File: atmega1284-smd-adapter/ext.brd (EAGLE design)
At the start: 37.6 x 55.9 mm, 5 parts

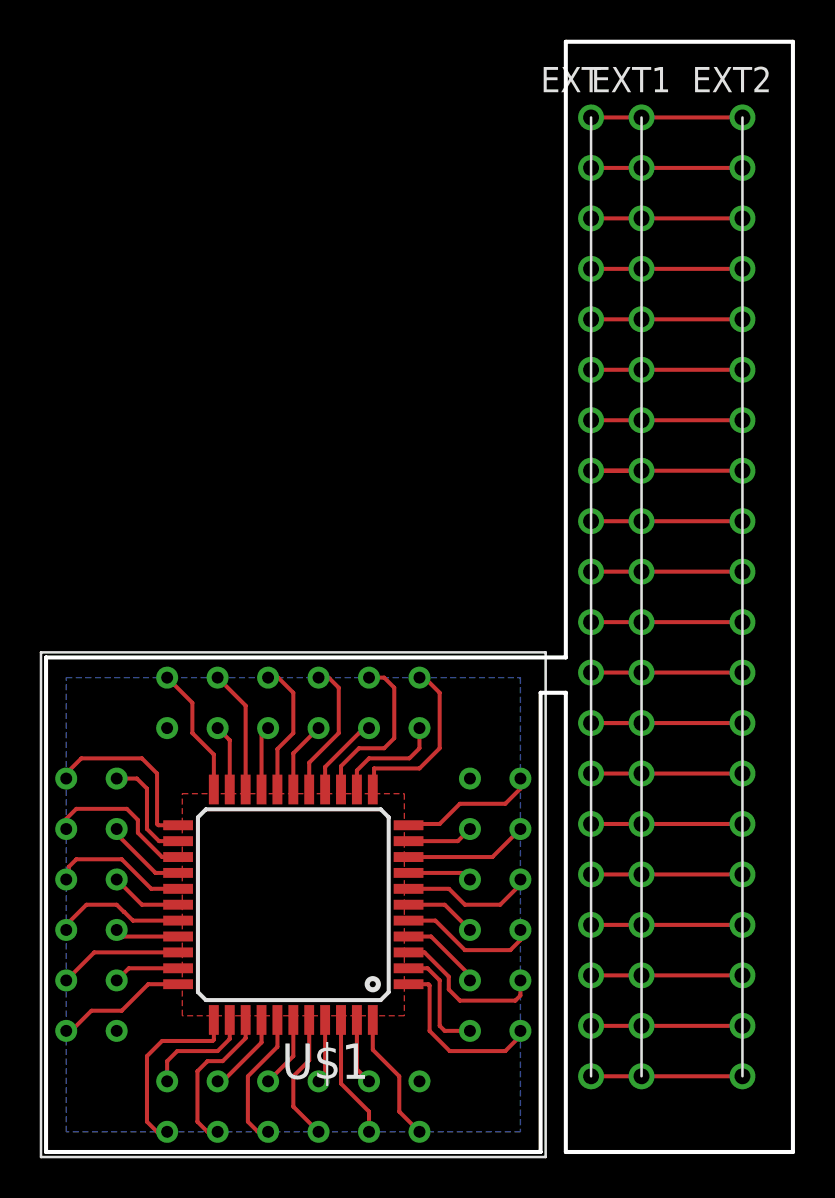
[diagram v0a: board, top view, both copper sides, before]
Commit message: [mk2 adapter split]
	- split the mk2-ext adapters into the actual mk2 extension board and
	  the atmega1284 smd adapter
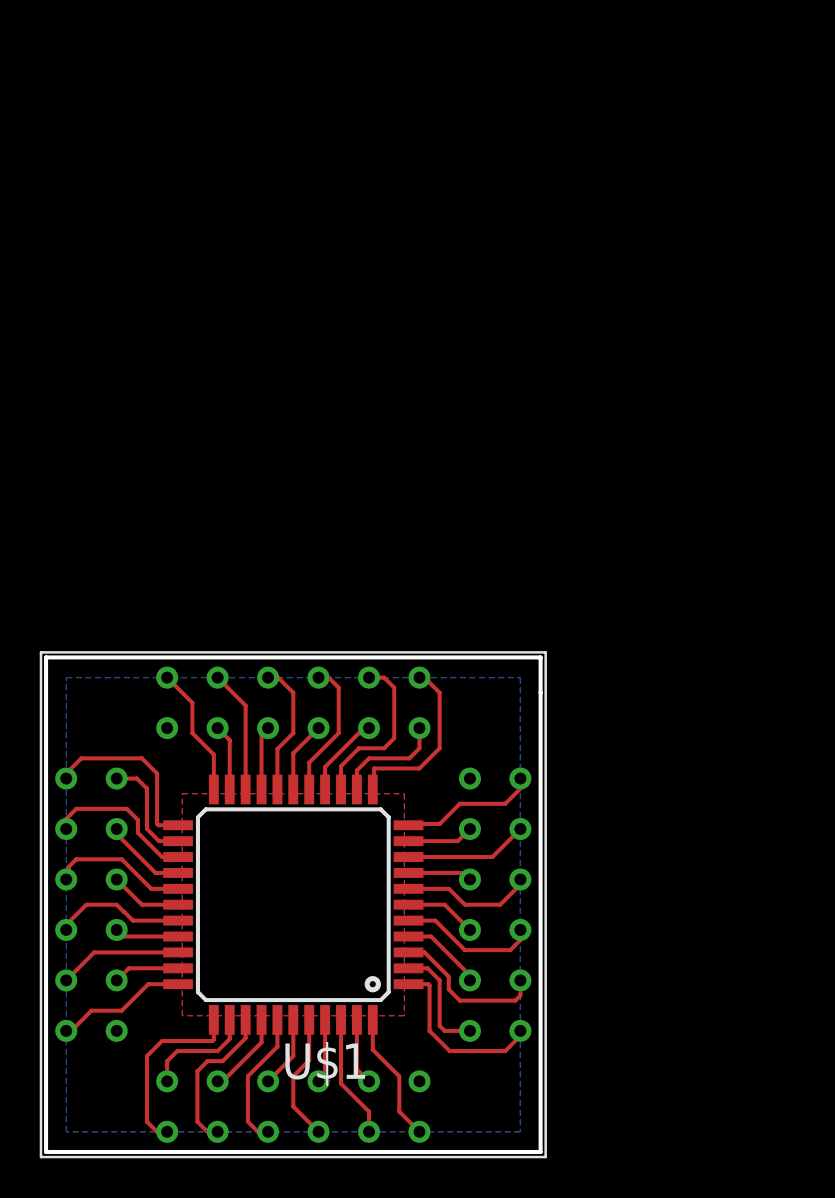
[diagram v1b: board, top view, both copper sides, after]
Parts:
- removed EXT, EXT1, EXT2: CON_DIL_20, connector:CON_DIL_20
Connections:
- removed net EXT_AIN0: EXT.P$8, EXT1.P$8, EXT2.P$8
- removed net EXT_GND0: EXT.P$9, EXT1.P$9, EXT2.P$9
- removed net EXT_GND1: EXT.P$19, EXT1.P$19, EXT2.P$19
- removed net EXT_MISO: EXT.P$5, EXT1.P$5, EXT2.P$5
- removed net EXT_MOSI: EXT.P$6, EXT1.P$6, EXT2.P$6
- removed net EXT_OC0A: EXT.P$15, EXT1.P$15, EXT2.P$15
- removed net EXT_OC0B: EXT.P$16, EXT1.P$16, EXT2.P$16
- removed net EXT_OC1A: EXT.P$17, EXT1.P$17, EXT2.P$17
- removed net EXT_OC1B: EXT.P$18, EXT1.P$18, EXT2.P$18
- removed net EXT_RX0: EXT.P$2, EXT1.P$2, EXT2.P$2
- removed net EXT_RX1: EXT.P$12, EXT1.P$12, EXT2.P$12
- removed net EXT_SCK: EXT.P$7, EXT1.P$7, EXT2.P$7
- removed net EXT_SCL0: EXT.P$3, EXT1.P$3, EXT2.P$3
- removed net EXT_SCL1: EXT.P$13, EXT1.P$13, EXT2.P$13
- removed net EXT_SDA0: EXT.P$4, EXT1.P$4, EXT2.P$4
- removed net EXT_SDA1: EXT.P$14, EXT1.P$14, EXT2.P$14
- removed net EXT_TX0: EXT.P$1, EXT1.P$1, EXT2.P$1
- removed net EXT_TX1: EXT.P$11, EXT1.P$11, EXT2.P$11
- removed net EXT_VCC0: EXT.P$10, EXT1.P$10, EXT2.P$10
- removed net EXT_VCC1: EXT.P$20, EXT1.P$20, EXT2.P$20
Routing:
- net EXT_SCL1: track 10.2 -> 0.00 mm
- net EXT_AIN0: track 10.2 -> 0.00 mm
- net EXT_VCC1: track 7.62 -> 0.00 mm
- net EXT_VCC0: track 7.62 -> 0.00 mm
- net EXT_TX1: track 7.62 -> 0.00 mm
- net EXT_TX0: track 7.62 -> 0.00 mm
- net EXT_SDA1: track 7.62 -> 0.00 mm
- net EXT_SDA0: track 7.62 -> 0.00 mm
- net EXT_SCL0: track 7.62 -> 0.00 mm
- net EXT_SCK: track 7.62 -> 0.00 mm
- net EXT_RX1: track 7.62 -> 0.00 mm
- net EXT_RX0: track 7.62 -> 0.00 mm
- net EXT_OC1B: track 7.62 -> 0.00 mm
- net EXT_OC1A: track 7.62 -> 0.00 mm
- net EXT_OC0B: track 7.62 -> 0.00 mm
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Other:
- board size 37.6 x 55.9 mm -> 24.9 x 24.9 mm
- board text removed: "AIN0"
- board text removed: "GND"
- board text removed: "MISO"
- board text removed: "MOSI"
- board text removed: "OC0A"
- board text removed: "OC0B"
- board text removed: "OC1A"
- board text removed: "OC1B"
- board text removed: "RX0"
- board text removed: "RX1"
- board text removed: "SCK"
- board text removed: "SCL"
- board text removed: "SDA"
- board text removed: "TX0"
- board text removed: "TX1"
- board text removed: "VCC"
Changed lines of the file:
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@@
 <board>
 <plain>
-<wire x1="54.61" y1="6.35" x2="66.04" y2="6.35" width="0.2032" layer="20"/>
-<text x="60.706" y="58.42" size="0.3048" layer="48" align="center-left">TX0</text>
-<text x="60.706" y="55.88" size="0.3048" layer="48" align="center-left">RX0</text>
-<text x="60.706" y="53.34" size="0.3048" layer="48" align="center-left">SCL</text>
-<text x="60.706" y="50.8" size="0.3048" layer="48" align="center-left">SDA</text>
-<text x="60.706" y="48.26" size="0.3048" layer="48" align="center-left">MISO</text>
-<text x="60.706" y="45.72" size="0.3048" layer="48" align="center-left">MOSI</text>
-<text x="60.706" y="43.18" size="0.3048" layer="48" align="center-left">SCK</text>
-<text x="60.706" y="40.64" size="0.3048" layer="48" align="center-left">AIN0</text>
-<text x="60.706" y="38.1" size="0.3048" layer="48" align="center-left">GND</text>
-<text x="60.706" y="35.56" size="0.3048" layer="48" align="center-left">VCC</text>
-<text x="60.706" y="33.02" size="0.3048" layer="48" align="center-left">TX1</text>
-<text x="60.706" y="30.48" size="0.3048" layer="48" align="center-left">RX1</text>
-<text x="60.706" y="27.94" size="0.3048" layer="48" align="center-left">SCL</text>
-<text x="60.706" y="25.4" size="0.3048" layer="48" align="center-left">SDA</text>
-<text x="60.706" y="22.86" size="0.3048" layer="48" align="center-left">OC0A</text>
-<text x="60.706" y="20.32" size="0.3048" layer="48" align="center-left">OC0B</text>
-<text x="60.706" y="17.78" size="0.3048" layer="48" align="center-left">OC1A</text>
-<text x="60.706" y="15.24" size="0.3048" layer="48" align="center-left">OC1B</text>
-<text x="60.706" y="12.7" size="0.3048" layer="48" align="center-left">GND</text>
-<text x="60.706" y="10.16" size="0.3048" layer="48" align="center-left">VCC</text>
-<wire x1="54.61" y1="62.23" x2="66.04" y2="62.23" width="0.2032" layer="20"/>
-<wire x1="66.04" y1="62.23" x2="66.04" y2="6.35" width="0.2032" layer="20"/>
-<wire x1="54.61" y1="62.23" x2="54.61" y2="31.242" width="0.2032" layer="20"/>
-<wire x1="54.61" y1="6.35" x2="54.61" y2="29.464" width="0.2032" layer="20"/>
-<wire x1="54.61" y1="29.464" x2="53.34" y2="29.464" width="0.2032" layer="20"/>
 <wire x1="53.34" y1="29.464" x2="53.34" y2="6.35" width="0.2032" layer="20"/>
 <wire x1="53.34" y1="6.35" x2="28.448" y2="6.35" width="0.2032" layer="20"/>
 <wire x1="28.448" y1="6.35" x2="28.448" y2="31.242" width="0.2032" layer="20"/>
-<wire x1="28.448" y1="31.242" x2="54.61" y2="31.242" width="0.2032" layer="20"/>
+<wire x1="28.448" y1="31.242" x2="53.34" y2="31.242" width="0.2032" layer="20"/>
+<wire x1="53.34" y1="31.242" x2="53.34" y2="29.464" width="0.2032" layer="20"/>
 </plain>
 <attributes>
@@
 </element>
 <element name="U$3" library="1284p.rpt" package="TQFP44-ADAPTER" value="MEGA1284P_ADAPTER" x="45.974" y="14.986" smashed="yes" rot="R180"/>
-<element name="EXT" library="connector" package="CON_DIL_20" value="CON_DIL_20" x="58.42" y="53.34" smashed="yes">
-<attribute name="NAME" x="53.34" y="59.69" size="1.27" layer="25"/>
-</element>
-<element name="EXT1" library="connector" package="CON_DIL_20" value="CON_DIL_20" x="60.96" y="53.34" smashed="yes">
-<attribute name="NAME" x="55.88" y="59.69" size="1.27" layer="25"/>
-</element>
-<element name="EXT2" library="connector" package="CON_DIL_20" value="CON_DIL_20" x="66.04" y="53.34" smashed="yes">
-<attribute name="NAME" x="60.96" y="59.69" size="1.27" layer="25"/>
-</element>
 </elements>
 <signals>
@@
 <wire x1="42.494" y1="10.236" x2="42.164" y2="9.906" width="0.2032" layer="1"/>
 </signal>
-<signal name="EXT_TX0">
-<contactref element="EXT" pad="P$1"/>
-<contactref element="EXT1" pad="P$1"/>
-<contactref element="EXT2" pad="P$1"/>
-<wire x1="55.88" y1="58.42" x2="58.42" y2="58.42" width="0.2032" layer="1"/>
-<wire x1="58.42" y1="58.42" x2="63.5" y2="58.42" width="0.2032" layer="1"/>
-</signal>
-<signal name="EXT_RX0">
-<contactref element="EXT" pad="P$2"/>
-<contactref element="EXT1" pad="P$2"/>
-<contactref element="EXT2" pad="P$2"/>
-<wire x1="55.88" y1="55.88" x2="58.42" y2="55.88" width="0.2032" layer="1"/>
-<wire x1="58.42" y1="55.88" x2="63.5" y2="55.88" width="0.2032" layer="1"/>
-</signal>
-<signal name="EXT_SCL1">
-<contactref element="EXT" pad="P$13"/>
-<contactref element="EXT1" pad="P$13"/>
-<contactref element="EXT2" pad="P$13"/>
-<wire x1="55.88" y1="27.94" x2="63.5" y2="27.94" width="0.2032" layer="1"/>
-<wire x1="58.42" y1="27.94" x2="55.88" y2="27.94" width="0.2032" layer="1"/>
-</signal>
-<signal name="EXT_SDA0">
-<contactref element="EXT" pad="P$4"/>
-<contactref element="EXT1" pad="P$4"/>
-<contactref element="EXT2" pad="P$4"/>
-<wire x1="55.88" y1="50.8" x2="58.42" y2="50.8" width="0.2032" layer="1"/>
-<wire x1="58.42" y1="50.8" x2="63.5" y2="50.8" width="0.2032" layer="1"/>
-</signal>
-<signal name="EXT_MISO">
-<contactref element="EXT" pad="P$5"/>
-<contactref element="EXT1" pad="P$5"/>
-<contactref element="EXT2" pad="P$5"/>
-<wire x1="55.88" y1="48.26" x2="58.42" y2="48.26" width="0.2032" layer="1"/>
-<wire x1="58.42" y1="48.26" x2="63.5" y2="48.26" width="0.2032" layer="1"/>
-</signal>
-<signal name="EXT_MOSI">
-<contactref element="EXT" pad="P$6"/>
-<contactref element="EXT1" pad="P$6"/>
-<contactref element="EXT2" pad="P$6"/>
-<wire x1="55.88" y1="45.72" x2="58.42" y2="45.72" width="0.2032" layer="1"/>
-<wire x1="58.42" y1="45.72" x2="63.5" y2="45.72" width="0.2032" layer="1"/>
-</signal>
-<signal name="EXT_SCK">
-<contactref element="EXT" pad="P$7"/>
-<contactref element="EXT1" pad="P$7"/>
-<contactref element="EXT2" pad="P$7"/>
-<wire x1="55.88" y1="43.18" x2="58.42" y2="43.18" width="0.2032" layer="1"/>
-<wire x1="58.42" y1="43.18" x2="63.5" y2="43.18" width="0.2032" layer="1"/>
-</signal>
-<signal name="EXT_AIN0">
-<contactref element="EXT" pad="P$8"/>
-<contactref element="EXT1" pad="P$8"/>
-<contactref element="EXT2" pad="P$8"/>
-<wire x1="55.88" y1="40.64" x2="63.5" y2="40.64" width="0.2032" layer="1"/>
-<wire x1="58.42" y1="40.64" x2="55.88" y2="40.64" width="0.2032" layer="1"/>
-</signal>
-<signal name="EXT_GND0">
-<contactref element="EXT" pad="P$9"/>
-<contactref element="EXT1" pad="P$9"/>
-<contactref element="EXT2" pad="P$9"/>
-<wire x1="58.42" y1="38.1" x2="63.5" y2="38.1" width="0.2032" layer="1"/>
-<wire x1="55.88" y1="38.1" x2="58.42" y2="38.1" width="0.2032" layer="1"/>
-</signal>
-<signal name="EXT_VCC0">
-<contactref element="EXT" pad="P$10"/>
-<contactref element="EXT1" pad="P$10"/>
-<contactref element="EXT2" pad="P$10"/>
-<wire x1="58.42" y1="35.56" x2="63.5" y2="35.56" width="0.2032" layer="1"/>
-<wire x1="55.88" y1="35.56" x2="58.42" y2="35.56" width="0.2032" layer="1"/>
-</signal>
-<signal name="EXT_TX1">
-<contactref element="EXT" pad="P$11"/>
-<contactref element="EXT1" pad="P$11"/>
-<contactref element="EXT2" pad="P$11"/>
-<wire x1="58.42" y1="33.02" x2="63.5" y2="33.02" width="0.2032" layer="1"/>
-<wire x1="55.88" y1="33.02" x2="58.42" y2="33.02" width="0.2032" layer="1"/>
-</signal>
-<signal name="EXT_RX1">
-<contactref element="EXT" pad="P$12"/>
-<contactref element="EXT1" pad="P$12"/>
-<contactref element="EXT2" pad="P$12"/>
-<wire x1="58.42" y1="30.48" x2="63.5" y2="30.48" width="0.2032" layer="1"/>
-<wire x1="55.88" y1="30.48" x2="58.42" y2="30.48" width="0.2032" layer="1"/>
-</signal>
-<signal name="EXT_SCL0">
-<contactref element="EXT" pad="P$3"/>
-<contactref element="EXT1" pad="P$3"/>
-<contactref element="EXT2" pad="P$3"/>
-<wire x1="55.88" y1="53.34" x2="58.42" y2="53.34" width="0.2032" layer="1"/>
-<wire x1="58.42" y1="53.34" x2="63.5" y2="53.34" width="0.2032" layer="1"/>
-</signal>
-<signal name="EXT_SDA1">
-<contactref element="EXT" pad="P$14"/>
-<contactref element="EXT1" pad="P$14"/>
-<contactref element="EXT2" pad="P$14"/>
-<wire x1="58.42" y1="25.4" x2="63.5" y2="25.4" width="0.2032" layer="1"/>
-<wire x1="55.88" y1="25.4" x2="58.42" y2="25.4" width="0.2032" layer="1"/>
-</signal>
-<signal name="EXT_OC0A">
-<contactref element="EXT" pad="P$15"/>
-<contactref element="EXT1" pad="P$15"/>
-<contactref element="EXT2" pad="P$15"/>
-<wire x1="58.42" y1="22.86" x2="63.5" y2="22.86" width="0.2032" layer="1"/>
-<wire x1="55.88" y1="22.86" x2="58.42" y2="22.86" width="0.2032" layer="1"/>
-</signal>
-<signal name="EXT_OC0B">
-<contactref element="EXT" pad="P$16"/>
-<contactref element="EXT1" pad="P$16"/>
-<contactref element="EXT2" pad="P$16"/>
-<wire x1="58.42" y1="20.32" x2="63.5" y2="20.32" width="0.2032" layer="1"/>
-<wire x1="55.88" y1="20.32" x2="58.42" y2="20.32" width="0.2032" layer="1"/>
-</signal>
-<signal name="EXT_OC1A">
-<contactref element="EXT" pad="P$17"/>
-<contactref element="EXT1" pad="P$17"/>
-<contactref element="EXT2" pad="P$17"/>
-<wire x1="58.42" y1="17.78" x2="63.5" y2="17.78" width="0.2032" layer="1"/>
-<wire x1="55.88" y1="17.78" x2="58.42" y2="17.78" width="0.2032" layer="1"/>
-</signal>
-<signal name="EXT_OC1B">
-<contactref element="EXT" pad="P$18"/>
-<contactref element="EXT1" pad="P$18"/>
-<contactref element="EXT2" pad="P$18"/>
-<wire x1="58.42" y1="15.24" x2="63.5" y2="15.24" width="0.2032" layer="1"/>
-<wire x1="55.88" y1="15.24" x2="58.42" y2="15.24" width="0.2032" layer="1"/>
-</signal>
-<signal name="EXT_GND1">
-<contactref element="EXT" pad="P$19"/>
-<contactref element="EXT1" pad="P$19"/>
-<contactref element="EXT2" pad="P$19"/>
-<wire x1="58.42" y1="12.7" x2="63.5" y2="12.7" width="0.2032" layer="1"/>
-<wire x1="55.88" y1="12.7" x2="58.42" y2="12.7" width="0.2032" layer="1"/>
-</signal>
-<signal name="EXT_VCC1">
-<contactref element="EXT" pad="P$20"/>
-<contactref element="EXT1" pad="P$20"/>
-<contactref element="EXT2" pad="P$20"/>
-<wire x1="58.42" y1="10.16" x2="63.5" y2="10.16" width="0.2032" layer="1"/>
-<wire x1="55.88" y1="10.16" x2="58.42" y2="10.16" width="0.2032" layer="1"/>
-</signal>
 </signals>
